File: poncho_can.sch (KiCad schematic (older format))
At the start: 40 parts, among them J10 GS2, J101 DB9_Male_MountingHoles, J102 DB9_Male_MountingHoles, J103 GS2, J104 GS2, J105 GS2, J106 GS2, J7 GS2, J8 GS2, J9 GS2, U101 TJA1051T, U102 TJA1051T

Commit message: Agrego el numero de parte de Digikey para todos los componentes
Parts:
- C101, C102, C103, C104: Digikey Part Number (none) -> 490-7227-1-ND
- C105, C106: Digikey Part Number (none) -> 311-4354-1-ND
- D101, D102: Digikey Part Number (none) -> ESD7002WTT1GOSCT-ND
- D103, D106: Digikey Part Number (none) -> 160-1427-1-ND
- D104, D105: Digikey Part Number (none) -> 160-1423-1-ND
- J101, J102: Digikey Part Number (none) -> 609-5183-ND
- R101, R102, R103, R104, R105, R106, R107, R108: Digikey Part Number (none) -> RMCF0805FT60R4CT-ND
- R109, R110, R111, R112: Digikey Part Number (none) -> RMCF0805JT270RCT-ND
- U101, U102: Digikey Part Number (none) -> 568-10292-1-ND
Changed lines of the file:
@@
 F 2 "Housings_SOIC:SOIC-8_3.9x4.9mm_Pitch1.27mm" H 6100 2200 50  0001 C CIN
 F 3 "" H 6100 2700 50  0001 C CNN
+F 4 "568-10292-1-ND" H 6100 2700 60  0001 C CNN "Digikey Part Number"
 	1    6100 2700
 	-1   0    0    -1
@@
 F 2 "Resistors_SMD:R_0805_HandSoldering" V 4680 2350 50  0001 C CNN
 F 3 "" H 4750 2350 50  0001 C CNN
+F 4 "RMCF0805FT60R4CT-ND" V 4750 2350 60  0001 C CNN "Digikey Part Number"
 	1    4750 2350
 	0    1    1    0
@@
 F 2 "Connect:DB9MC" H 2150 2700 50  0001 C CNN
 F 3 "" H 2150 2700 50  0001 C CNN
+F 4 "609-5183-ND" H 2150 2700 60  0001 C CNN "Digikey Part Number"
 	1    2150 2700
 	-1   0    0    -1
@@
 F 2 "Resistors_SMD:R_0805_HandSoldering" V 4280 2350 50  0001 C CNN
 F 3 "" H 4350 2350 50  0001 C CNN
+F 4 "RMCF0805FT60R4CT-ND" V 4350 2350 60  0001 C CNN "Digikey Part Number"
 	1    4350 2350
 	0    1    1    0
@@
 F 2 "Resistors_SMD:R_0805_HandSoldering" V 4680 2900 50  0001 C CNN
 F 3 "" H 4750 2900 50  0001 C CNN
+F 4 "RMCF0805FT60R4CT-ND" V 4750 2900 60  0001 C CNN "Digikey Part Number"
 	1    4750 2900
 	0    1    1    0
@@
 F 2 "Resistors_SMD:R_0805_HandSoldering" V 4280 2900 50  0001 C CNN
 F 3 "" H 4350 2900 50  0001 C CNN
+F 4 "RMCF0805FT60R4CT-ND" V 4350 2900 60  0001 C CNN "Digikey Part Number"
 	1    4350 2900
 	0    1    1    0
@@
 F 2 "Capacitors_SMD:C_0805_HandSoldering" H 4588 1900 50  0001 C CNN
 F 3 "" H 4550 2050 50  0001 C CNN
+F 4 "490-7227-1-ND" H 4550 2050 60  0001 C CNN "Digikey Part Number"
 	1    4550 2050
 	1    0    0    -1
@@
 F 2 "Capacitors_SMD:C_0805_HandSoldering" H 4588 3000 50  0001 C CNN
 F 3 "" H 4550 3150 50  0001 C CNN
+F 4 "490-7227-1-ND" H 4550 3150 60  0001 C CNN "Digikey Part Number"
 	1    4550 3150
 	1    0    0    -1
@@
 F 2 "Capacitors_SMD:C_0805_HandSoldering" H 6688 1750 50  0001 C CNN
 F 3 "" H 6650 1900 50  0001 C CNN
+F 4 "311-4354-1-ND" H 6650 1900 60  0001 C CNN "Digikey Part Number"
 	1    6650 1900
 	1    0    0    -1
@@
 F 2 "TO_SOT_Packages_SMD:SOT-23W_Handsoldering" H 3150 2600 50  0001 C CNN
 F 3 "" H 3150 2600 50  0001 C CNN
+F 4 "ESD7002WTT1GOSCT-ND" H 3300 2600 60  0001 C CNN "Digikey Part Number"
 	1    3300 2600
 	0    1    -1   0
@@
 F 2 "Housings_SOIC:SOIC-8_3.9x4.9mm_Pitch1.27mm" H 6100 4150 50  0001 C CIN
 F 3 "" H 6100 4650 50  0001 C CNN
+F 4 "568-10292-1-ND" H 6100 4650 60  0001 C CNN "Digikey Part Number"
 	1    6100 4650
 	-1   0    0    -1
@@
 F 2 "Resistors_SMD:R_0805_HandSoldering" V 4680 4300 50  0001 C CNN
 F 3 "" H 4750 4300 50  0001 C CNN
+F 4 "RMCF0805FT60R4CT-ND" V 4750 4300 60  0001 C CNN "Digikey Part Number"
 	1    4750 4300
 	0    1    1    0
@@
 F 2 "Connect:DB9MC" H 2150 4650 50  0001 C CNN
 F 3 "" H 2150 4650 50  0001 C CNN
+F 4 "609-5183-ND" H 2150 4650 60  0001 C CNN "Digikey Part Number"
 	1    2150 4650
 	-1   0    0    -1
@@
 F 2 "Resistors_SMD:R_0805_HandSoldering" V 4280 4300 50  0001 C CNN
 F 3 "" H 4350 4300 50  0001 C CNN
+F 4 "RMCF0805FT60R4CT-ND" V 4350 4300 60  0001 C CNN "Digikey Part Number"
 	1    4350 4300
 	0    1    1    0
@@
 F 2 "Resistors_SMD:R_0805_HandSoldering" V 4680 4850 50  0001 C CNN
 F 3 "" H 4750 4850 50  0001 C CNN
+F 4 "RMCF0805FT60R4CT-ND" V 4750 4850 60  0001 C CNN "Digikey Part Number"
 	1    4750 4850
 	0    1    1    0
@@
 F 2 "Resistors_SMD:R_0805_HandSoldering" V 4280 4850 50  0001 C CNN
 F 3 "" H 4350 4850 50  0001 C CNN
+F 4 "RMCF0805FT60R4CT-ND" V 4350 4850 60  0001 C CNN "Digikey Part Number"
 	1    4350 4850
 	0    1    1    0
@@
 F 2 "Capacitors_SMD:C_0805_HandSoldering" H 4588 3850 50  0001 C CNN
 F 3 "" H 4550 4000 50  0001 C CNN
+F 4 "490-7227-1-ND" H 4550 4000 60  0001 C CNN "Digikey Part Number"
 	1    4550 4000
 	1    0    0    -1
@@
 F 2 "Capacitors_SMD:C_0805_HandSoldering" H 4588 4950 50  0001 C CNN
 F 3 "" H 4550 5100 50  0001 C CNN
+F 4 "490-7227-1-ND" H 4550 5100 60  0001 C CNN "Digikey Part Number"
 	1    4550 5100
 	1    0    0    -1
@@
 F 2 "Capacitors_SMD:C_0805_HandSoldering" H 6688 3750 50  0001 C CNN
 F 3 "" H 6650 3900 50  0001 C CNN
+F 4 "311-4354-1-ND" H 6650 3900 60  0001 C CNN "Digikey Part Number"
 	1    6650 3900
 	1    0    0    -1
@@
 F 2 "TO_SOT_Packages_SMD:SOT-23W_Handsoldering" H 3150 4550 50  0001 C CNN
 F 3 "" H 3150 4550 50  0001 C CNN
+F 4 "ESD7002WTT1GOSCT-ND" H 3300 4550 60  0001 C CNN "Digikey Part Number"
 	1    3300 4550
 	0    1    -1   0
@@
 F 2 "LEDs:LED_0805_HandSoldering" H 7150 2150 50  0001 C CNN
 F 3 "" H 7150 2150 50  0001 C CNN
+F 4 "160-1427-1-ND " H 7150 2150 60  0001 C CNN "Digikey Part Number"
 	1    7150 2150
 	0    -1   -1   0
@@
 F 2 "LEDs:LED_0805_HandSoldering" H 7500 2150 50  0001 C CNN
 F 3 "" H 7500 2150 50  0001 C CNN
+F 4 "160-1423-1-ND " H 7500 2150 60  0001 C CNN "Digikey Part Number"
 	1    7500 2150
 	0    -1   -1   0
@@
 F 2 "Resistors_SMD:R_0805_HandSoldering" V 7080 1800 50  0001 C CNN
 F 3 "" H 7150 1800 50  0001 C CNN
+F 4 "RMCF0805JT270RCT-ND " V 7150 1800 60  0001 C CNN "Digikey Part Number"
 	1    7150 1800
 	-1   0    0    1
@@
 F 2 "Resistors_SMD:R_0805_HandSoldering" V 7430 1800 50  0001 C CNN
 F 3 "" H 7500 1800 50  0001 C CNN
+F 4 "RMCF0805JT270RCT-ND " V 7500 1800 60  0001 C CNN "Digikey Part Number"
 	1    7500 1800
 	-1   0    0    1
@@
 F 2 "LEDs:LED_0805_HandSoldering" H 7150 4100 50  0001 C CNN
 F 3 "" H 7150 4100 50  0001 C CNN
+F 4 "160-1423-1-ND " H 7150 4100 60  0001 C CNN "Digikey Part Number"
 	1    7150 4100
 	0    -1   -1   0
@@
 F 2 "LEDs:LED_0805_HandSoldering" H 7500 4100 50  0001 C CNN
 F 3 "" H 7500 4100 50  0001 C CNN
+F 4 "160-1427-1-ND " H 7500 4100 60  0001 C CNN "Digikey Part Number"
 	1    7500 4100
 	0    -1   -1   0
@@
 F 2 "Resistors_SMD:R_0805_HandSoldering" V 7080 3750 50  0001 C CNN
 F 3 "" H 7150 3750 50  0001 C CNN
+F 4 "RMCF0805JT270RCT-ND " V 7150 3750 60  0001 C CNN "Digikey Part Number"
 	1    7150 3750
 	-1   0    0    1
@@
 F 2 "Resistors_SMD:R_0805_HandSoldering" V 7430 3750 50  0001 C CNN
 F 3 "" H 7500 3750 50  0001 C CNN
+F 4 "RMCF0805JT270RCT-ND " V 7500 3750 60  0001 C CNN "Digikey Part Number"
 	1    7500 3750
 	-1   0    0    1

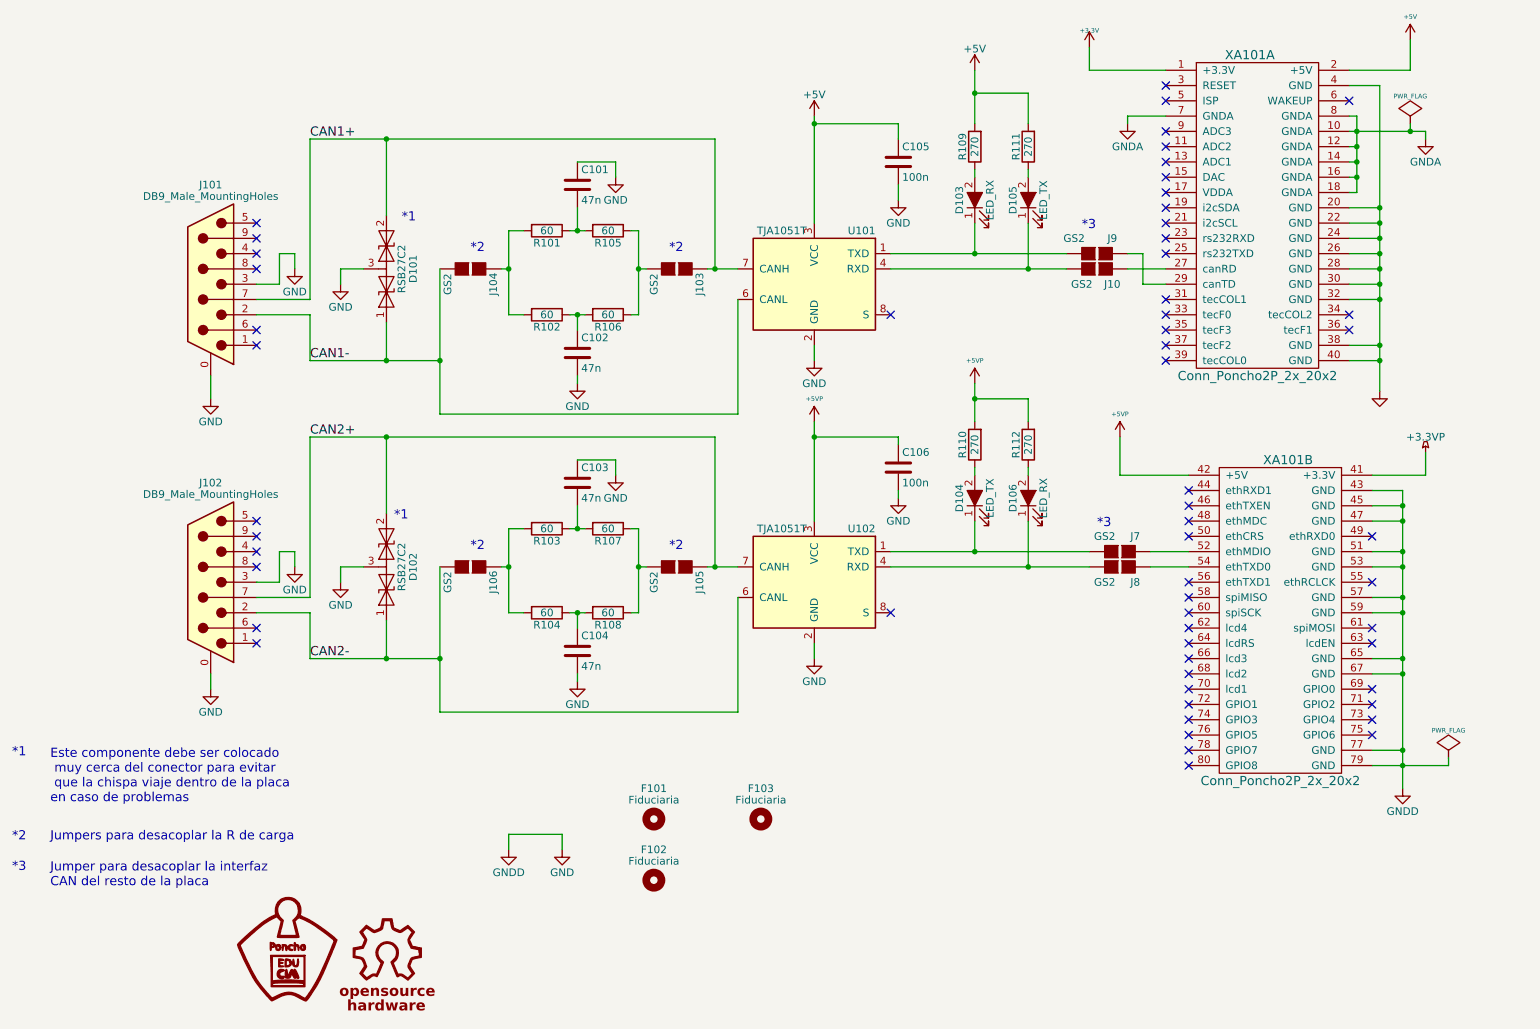
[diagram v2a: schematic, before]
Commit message: Cambio el esquematico para poder capturar la pantalla y usarla en la memoria
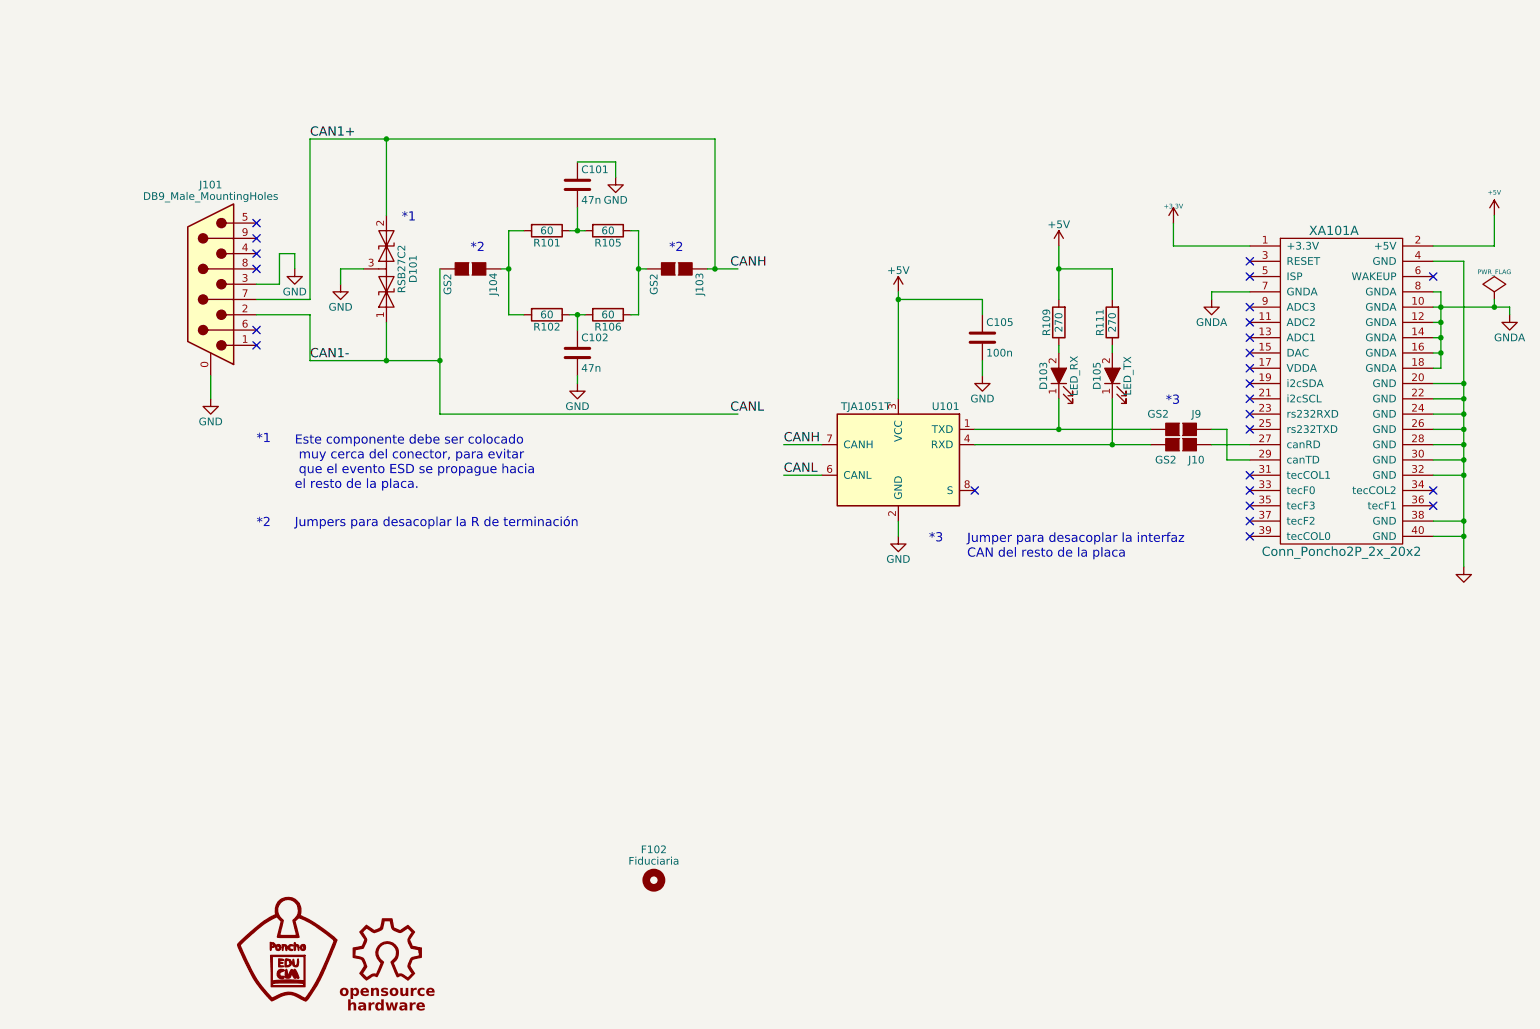
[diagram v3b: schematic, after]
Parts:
- removed C103, C104: 47n, Capacitors_SMD:C_0805_HandSoldering, symbol C
- removed C106: 100n, Capacitors_SMD:C_0805_HandSoldering, symbol C
- removed D102: RSB27C2, TO_SOT_Packages_SMD:SOT-23W_Handsoldering, symbol A00094
- removed D104: LED_TX, LEDs:LED_0805_HandSoldering, symbol LED_ALT
- removed D106: LED_RX, LEDs:LED_0805_HandSoldering, symbol LED_ALT
- removed F101, F103: Fiduciaria, Fiducials:Fiducial_1mm_Dia_2.54mm_Outer_CopperBottom, symbol Mounting_Hole
- removed J102: DB9_Male_MountingHoles, Connect:DB9MC, symbol DB9_Male_MountingHoles
- removed J105, J106, J7, J8: GS2, Connect:GS2, symbol GS2
- removed R103, R104, R107, R108: 60, Resistors_SMD:R_0805_HandSoldering, symbol R
- removed R110, R112: 270, Resistors_SMD:R_0805_HandSoldering, symbol R
- removed U102: TJA1051T, Housings_SOIC:SOIC-8_3.9x4.9mm_Pitch1.27mm, symbol TJA1051T
- removed unit 2 of XA101
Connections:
- no-connect marks 58 -> 26
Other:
- note added: "Este componente debe ser colocado\n muy cerca del conector, para evitar\n que el evento ESD se propague hacia \nel resto de la placa."
- note added: "Jumpers para desacoplar la R de terminación"
- note removed: "Este componente debe ser colocado\n muy cerca del conector para evitar\n que la chispa viaje dentro de la placa \nen caso de problemas"
- note removed: "Jumpers para desacoplar la R de carga"
- moved on the sheet: C105, D103, D105, J10, J9, R109, R111, U101, XA101A
